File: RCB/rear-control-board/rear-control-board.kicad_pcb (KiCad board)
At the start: 2 copper layers, 53 parts, among them J1 Conn_01x23, J2 Conn_01x14, J3 Conn_01x08, J4 Conn_01x02, J5 Conn_01x02, J6 Conn_01x05, K1 T9VV1K15-12S, K2 G5V-2, K3 G5V-2, Q1 BSS84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

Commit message: working on layout
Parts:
- moved J3 161.0 mm to (97.5, 49.5), turned to 180 degrees
- moved F1 119.5 mm to (127.8, 72.1)
- moved F8 119.0 mm to (137.7, 97.6), turned to 180 degrees
- moved J2 111.4 mm to (145.0, 49.8), turned to 180 degrees
- moved C1 109.3 mm to (243.8, 101.6)
- moved C10 109.3 mm to (234.4, 103.4)
- moved C11 109.3 mm to (243.8, 94.1)
- moved C12 109.3 mm to (230.1, 103.4)
- moved C2 109.3 mm to (252.8, 93.9)
- moved C3 109.3 mm to (248.2, 96.4)
- moved C4 109.3 mm to (243.8, 99.1)
- moved C5 109.3 mm to (252.8, 91.4)
- moved C6 109.3 mm to (243.8, 96.6)
- moved C7 109.3 mm to (238.8, 103.4)
- moved C8 109.3 mm to (248.4, 93.9)
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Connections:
- F8 pad 1: +12V -> /SSOK
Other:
- board outline added: 99.1 x 99.1 mm

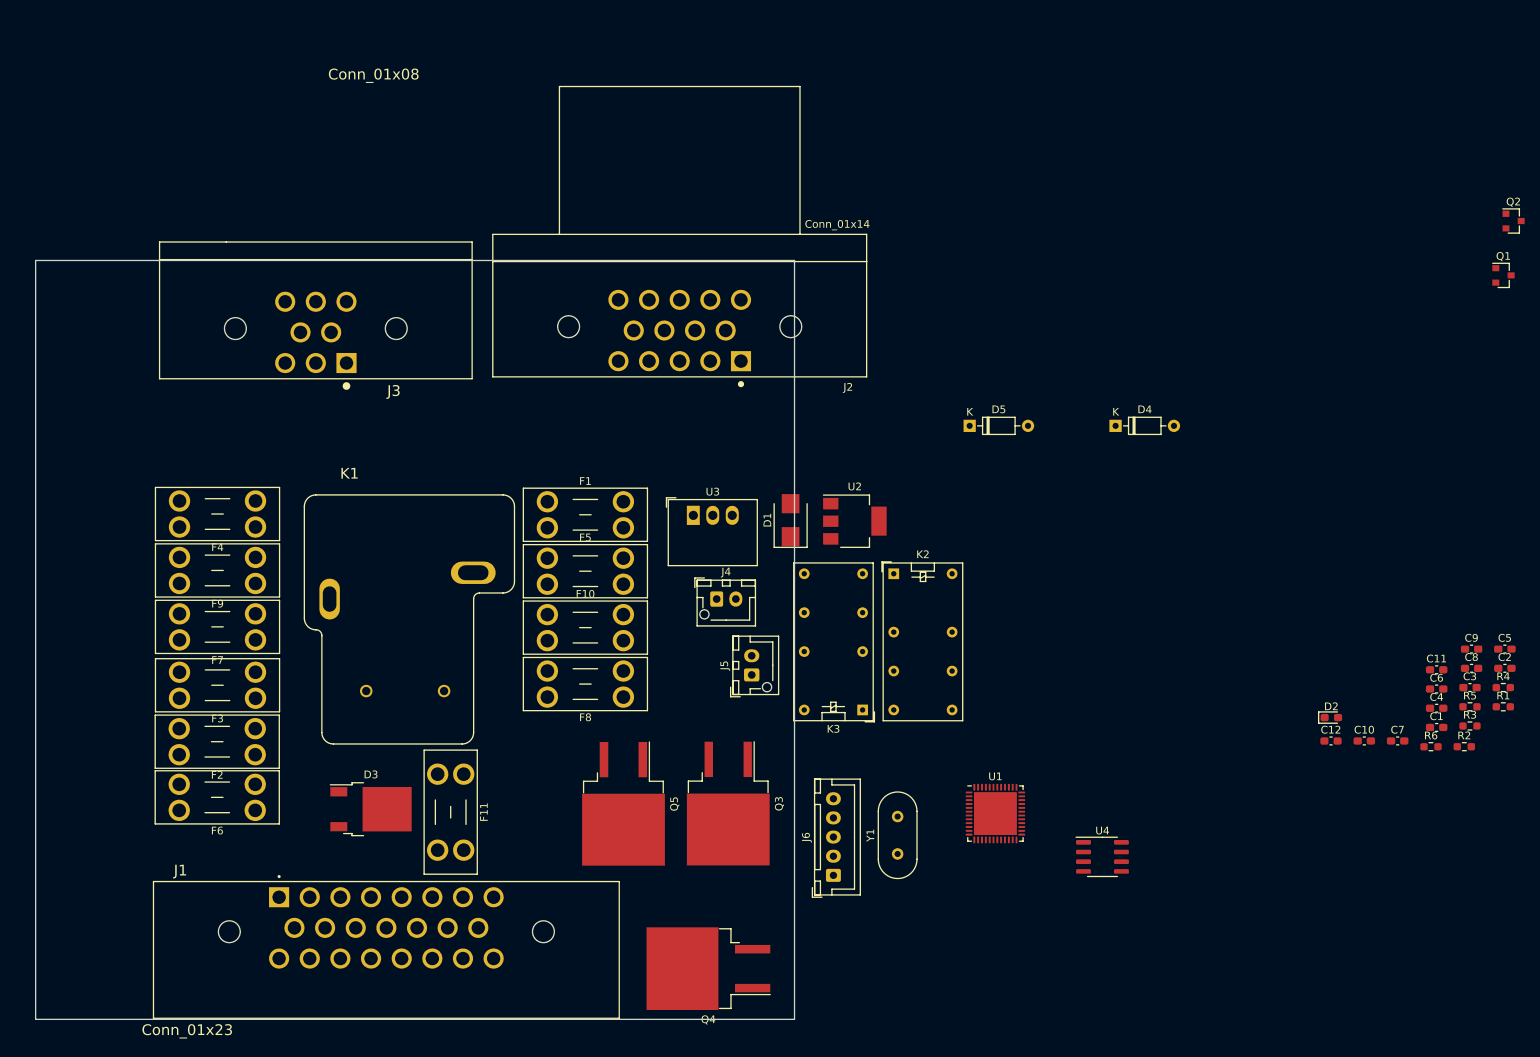
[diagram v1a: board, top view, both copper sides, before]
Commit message: layout and connector pins
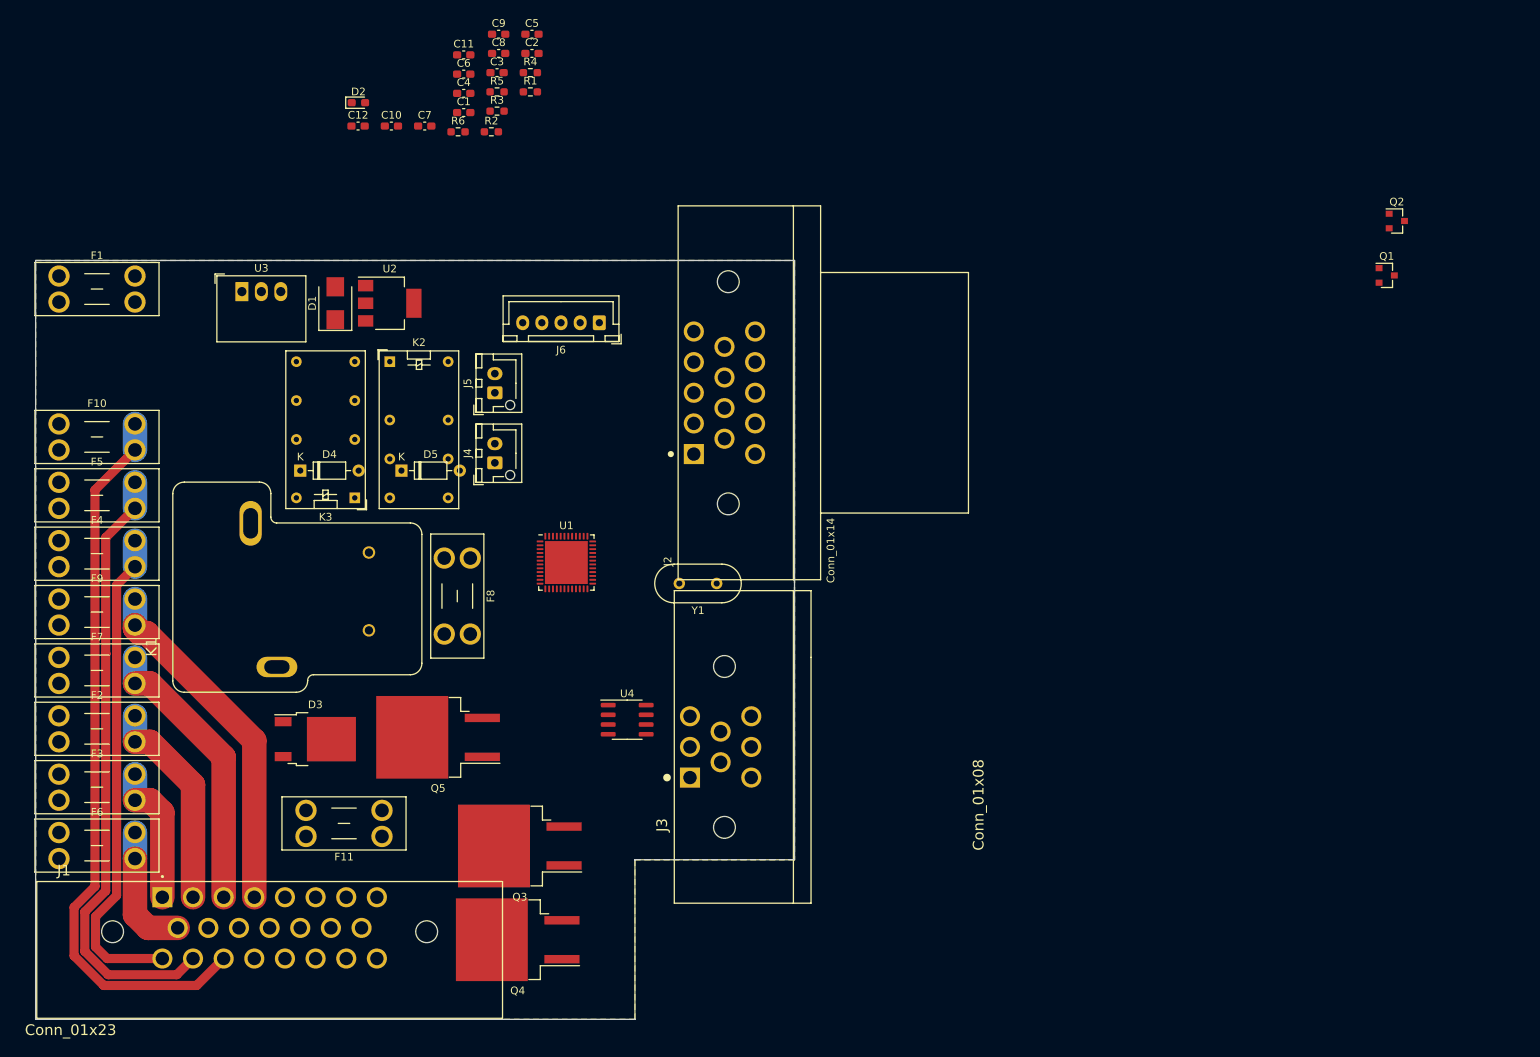
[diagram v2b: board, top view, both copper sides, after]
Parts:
- moved C12 150.2 mm to (103.0, 23.1)
- moved C1 150.2 mm to (116.8, 21.3)
- moved C10 150.2 mm to (107.4, 23.1)
- moved C11 150.2 mm to (116.8, 13.8)
- moved C2 150.2 mm to (125.8, 13.6)
- moved C3 150.2 mm to (121.2, 16.1)
- moved C4 150.2 mm to (116.8, 18.8)
- moved C5 150.2 mm to (125.8, 11.1)
- moved C6 150.2 mm to (116.8, 16.3)
- moved C7 150.2 mm to (111.8, 23.1)
- moved C8 150.2 mm to (121.4, 13.6)
- moved C9 150.2 mm to (121.4, 11.1)
- moved D2 150.2 mm to (103.1, 20.0)
- moved R1 150.2 mm to (125.5, 18.6)
- moved R2 150.2 mm to (120.5, 23.8)
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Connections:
- J1 pad 1: +12VA -> /RINEHART
- J1 pad 10: /PUMP_12V -> /FAULT_IMD
- J1 pad 11: /PUMP_SIG -> +12VA
- J1 pad 12: /RINEHART -> +12VA
- J1 pad 13: /DASH -> /DCDC_IN
- J1 pad 14: /HVB_12V -> /DCDC_IN
- J1 pad 15: /SPARE -> /PUMP_SIG
- J1 pad 16: /TSV -> /DASH
- J1 pad 17: /BRB -> /HVB_12V
- J1 pad 18: /BRB_RTN -> /BRB
- J1 pad 19: /FAULT_IMD -> /BRB_RTN
- J1 pad 2: +12VA -> /FAN_12V
- J1 pad 20: /FAULT_BMS -> GND
- J1 pad 21: Net-(J1-Pad21) -> GND
- J1 pad 22: GND -> /FAULT_BMS
- J1 pad 23: GND -> /TSV
- J1 pad 3: /DCDC_IN -> /SPARE
- J1 pad 4: /DCDC_IN -> /BRAKE_12V
- J1 pad 5: /DCDC_IN -> +12VA
- J1 pad 6: /FAN_12V -> /DCDC_IN
- J1 pad 7: /FAN_SIG -> /BRAKE_SIG
- J1 pad 8: /BRAKE_12V -> /FAN_SIG
- J1 pad 9: /BRAKE_SIG -> /PUMP_12V
- J3 pad 1: /CAN_P -> Net-(J3-Pad1)
- J3 pad 2: /CAN_P -> /CAN_N
- J3 pad 3: /CAN_N -> /CAN_P
- J3 pad 5: Net-(J3-Pad5) -> /CAN_P
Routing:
- net /BRB: track 0.00 -> 95.3 mm
- net /HVB_12V: track 0.00 -> 80.2 mm
- net /DASH: track 0.00 -> 64.5 mm
- net /BRAKE_12V: track 0.00 -> 45.9 mm
- net /SPARE: track 0.00 -> 37.3 mm
- net /FAN_12V: track 0.00 -> 28.0 mm
- net /RINEHART: track 0.00 -> 18.7 mm
- net /PUMP_12V: track 0.00 -> 17.0 mm
- added copper zone on B.Cu, net GND
- added copper zone on F.Cu, net GND
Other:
- outline, holes or cut-outs redrawn

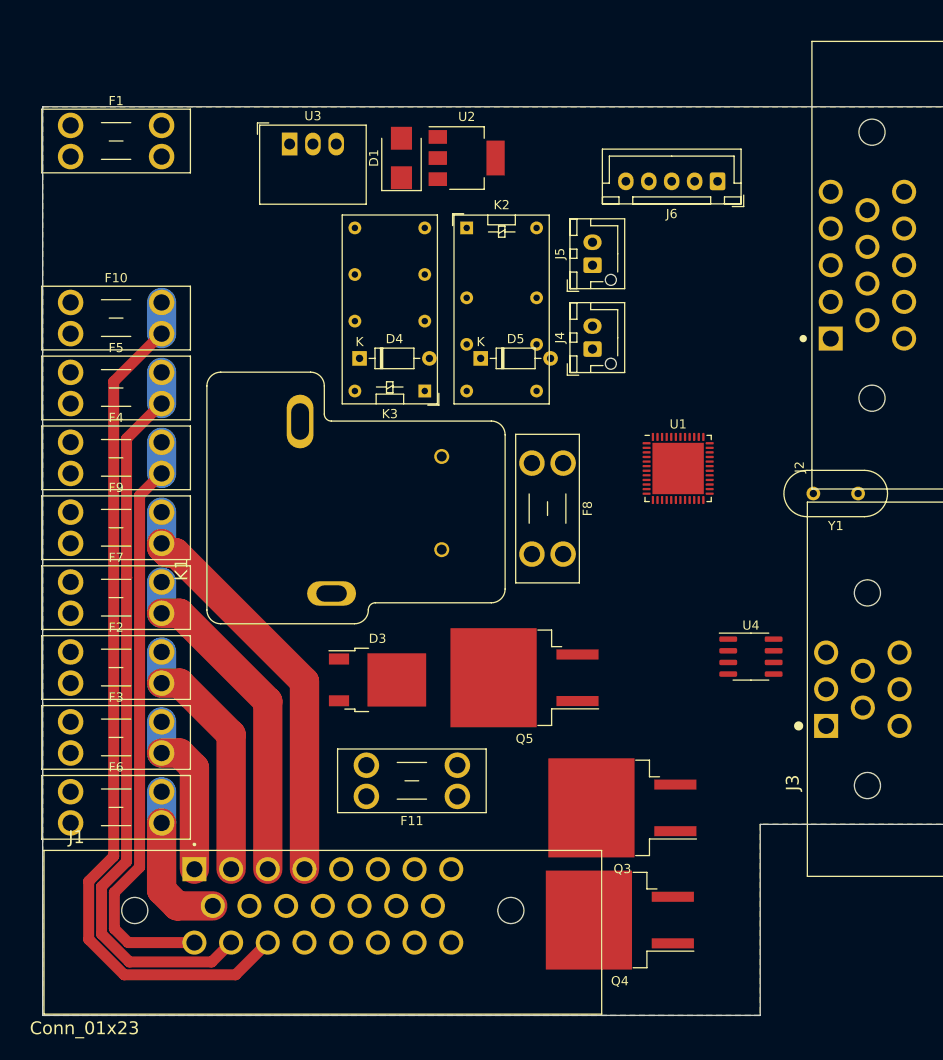
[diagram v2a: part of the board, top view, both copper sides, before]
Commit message: working on layout
Updating traces for RCB and organizing HVB
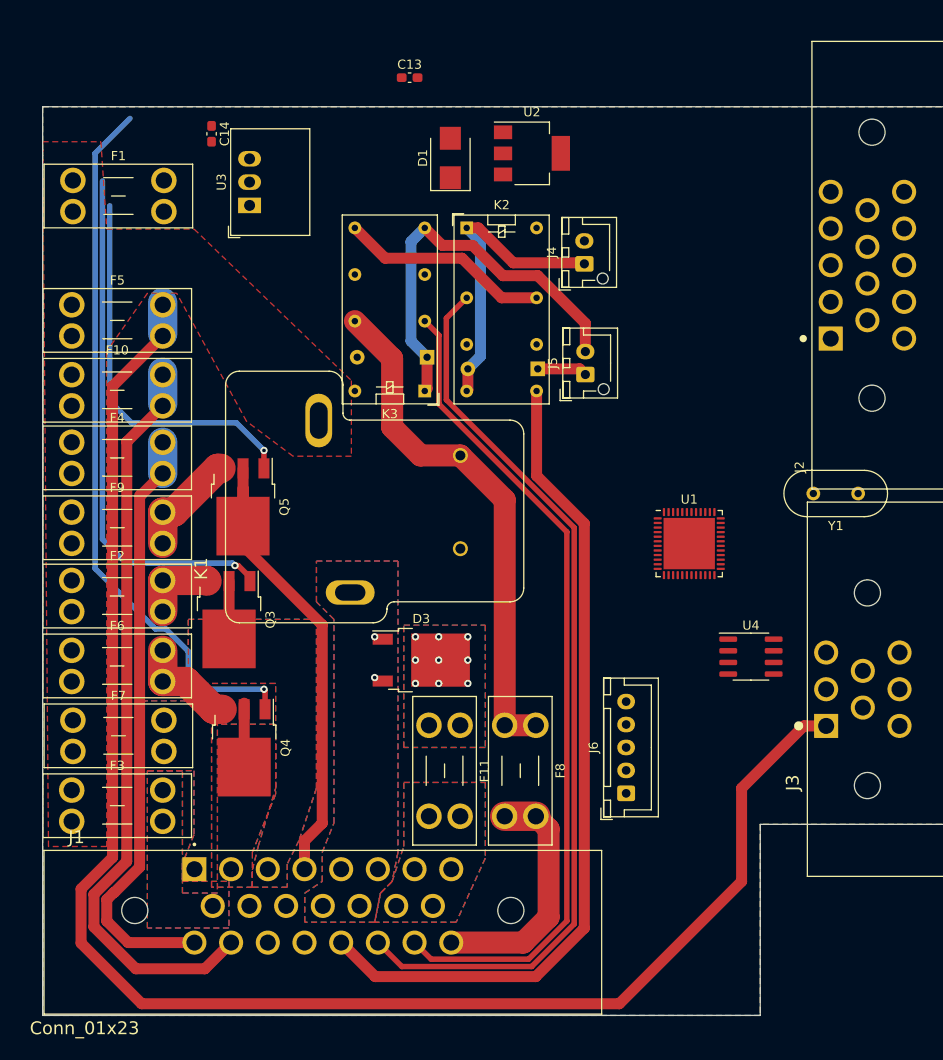
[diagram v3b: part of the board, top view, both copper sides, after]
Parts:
- added C13: C, Capacitor_SMD:C_0603_1608Metric_Pad1.08x0.95mm_HandSolder, F.Cu at (101.0, 37.5)
- added C14: C, Capacitor_SMD:C_0603_1608Metric_Pad1.08x0.95mm_HandSolder, F.Cu at (79.4, 43.6)
- D4, D5: moved to B.Cu
- Q3, Q4, Q5: value STB15N80K5 -> Q_PMOS_GDSD; footprint Package_TO_SOT_SMD:TO-263-2 -> Package_TO_SOT_SMD:TO-252-3_TabPin4
- moved J6 67.5 mm to (124.6, 115.5), turned to 90 degrees
- moved Q3 47.5 mm to (81.3, 96.6), turned to -90 degrees
- moved Q4 45.1 mm to (82.9, 110.5), turned to -90 degrees
- moved Q5 35.9 mm to (82.8, 84.3), turned to -90 degrees
- moved F8 28.7 mm to (114.7, 108.1)
- moved D4 19.5 mm to (114.9, 69.2), turned to 180 degrees
- moved F6 15.4 mm to (64.1, 99.9)
- moved F7 15.1 mm to (64.3, 107.5)
- moved J5 11.9 mm to (120.1, 69.8)
- moved J4 9.33 mm to (120.0, 57.8)
- moved U1 8.28 mm to (131.4, 88.3)
- moved U3 7.99 mm to (83.5, 51.4), turned to 90 degrees
- moved F10 7.87 mm to (64.1, 69.8)
- moved F2 7.80 mm to (64.1, 92.3)
- moved F11 7.76 mm to (106.5, 108.1), turned to -90 degrees
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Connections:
- net /FAULT_LATCHER/BMS_IND renamed /Controller/FAULT_BMS
- net Net-(D3-Pad2) renamed /charge-controller/dcdc_fuse
- net Net-(D4-Pad2) renamed /FAULT_LATCHER/bms_switch
- net Net-(D5-Pad1) renamed /FAULT_LATCHER/imd_switch
- net Net-(J3-Pad6) renamed /NC
- net Net-(K2-Pad13) renamed /FAULT_LATCHER/connector
- J1 pad 1: /RINEHART -> /SPARE
- J1 pad 10: /FAULT_IMD -> GND
- J1 pad 11: +12VA -> GND
- J1 pad 13: /DCDC_IN -> +12VA
- J1 pad 15: /PUMP_SIG -> /DCDC_IN
- J1 pad 17: /HVB_12V -> /BRB
- J1 pad 18: /BRB -> GND
- J1 pad 19: /BRB_RTN -> GND
- J1 pad 2: /FAN_12V -> /PUMP_CTRL_12V
- J1 pad 20: GND -> /BRB_RTN
- J1 pad 21: GND -> /FAULT_IMD
- J1 pad 3: /SPARE -> /FAN_CTRL_12V
- J1 pad 4: /BRAKE_12V -> /BRAKE_CTRL_12V
- J1 pad 6: /DCDC_IN -> +12VA
- J1 pad 7: /BRAKE_SIG -> /DCDC_IN
- J1 pad 8: /FAN_SIG -> /DCDC_IN
- J1 pad 9: /PUMP_12V -> /RINEHART
- J2 pad 13: +5V -> VDD
- J2 pad 14: +5V -> VDD
- J2 pad 5: GND -> unconnected-(J2-Pad5)
- J2 pad 6: +3V3 -> /TEMP_WATER
- J3 pad 1: Net-(J3-Pad1) -> /HVB_12V
- J3 pad 7: Net-(J3-Pad7) -> GND
- J3 pad 8: Net-(J3-Pad8) -> GND
- K2 pad 11: Net-(K2-Pad11) -> unconnected-(K2-Pad11)
- K2 pad 6: Net-(K2-Pad6) -> unconnected-(K2-Pad6)
- K3 pad 11: Net-(K3-Pad11) -> unconnected-(K3-Pad11)
- K3 pad 6: Net-(K3-Pad6) -> unconnected-(K3-Pad6)
- Q3 pad 2: /FAN_SIG -> /FAN_CTRL_12V
- Q3 pad 3: GND -> /FAN_12V
- Q4 pad 2: /PUMP_SIG -> /PUMP_CTRL_12V
- Q4 pad 3: GND -> /PUMP_12V
- Q5 pad 2: /BRAKE_SIG -> /BRAKE_CTRL_12V
- Q5 pad 3: GND -> /BRAKE_12V
- U1 pad 1: Net-(U1-Pad1) -> unconnected-(U1-Pad1)
- U1 pad 17: +3V3 -> /Controller/NTC1
- U1 pad 18: Net-(U1-Pad18) -> unconnected-(U1-Pad18)
- U1 pad 19: Net-(U1-Pad19) -> unconnected-(U1-Pad19)
- U1 pad 2: Net-(U1-Pad2) -> unconnected-(U1-Pad2)
- U1 pad 20: Net-(U1-Pad20) -> unconnected-(U1-Pad20)
- U1 pad 21: Net-(U1-Pad21) -> unconnected-(U1-Pad21)
- U1 pad 22: Net-(U1-Pad22) -> unconnected-(U1-Pad22)
- U1 pad 25: Net-(U1-Pad25) -> unconnected-(U1-Pad25)
- U1 pad 26: Net-(U1-Pad26) -> unconnected-(U1-Pad26)
- U1 pad 27: Net-(U1-Pad27) -> unconnected-(U1-Pad27)
- U1 pad 28: Net-(U1-Pad28) -> unconnected-(U1-Pad28)
- U1 pad 29: Net-(U1-Pad29) -> unconnected-(U1-Pad29)
- U1 pad 3: Net-(U1-Pad3) -> unconnected-(U1-Pad3)
- U1 pad 30: Net-(U1-Pad30) -> unconnected-(U1-Pad30)
- U1 pad 31: Net-(U1-Pad31) -> unconnected-(U1-Pad31)
- U1 pad 32: Net-(U1-Pad32) -> unconnected-(U1-Pad32)
- U1 pad 33: Net-(U1-Pad33) -> unconnected-(U1-Pad33)
- U1 pad 4: Net-(U1-Pad4) -> unconnected-(U1-Pad4)
- U1 pad 40: Net-(U1-Pad40) -> unconnected-(U1-Pad40)
- U1 pad 41: Net-(U1-Pad41) -> unconnected-(U1-Pad41)
- U1 pad 42: Net-(U1-Pad42) -> unconnected-(U1-Pad42)
- U1 pad 46: Net-(U1-Pad46) -> unconnected-(U1-Pad46)
- U1 pad 8: Net-(U1-Pad8) -> unconnected-(U1-Pad8)
- U4 pad 5: Net-(U4-Pad5) -> unconnected-(U4-Pad5)
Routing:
- net /FAULT_IMD: track 0.00 -> 99.4 mm
- net /HVB_12V: track 80.2 -> 175.7 mm
- net /BRB_RTN: track 0.00 -> 90.9 mm
- net /FAULT_BMS: track 0.00 -> 90.9 mm
- net /Controller/PUMP_CTRL: track 0.00 -> 78.0 mm, vias 0 -> 1
- net /Controller/FAN_CTRL: track 0.00 -> 57.3 mm, vias 0 -> 1
- net /SSOK: track 0.00 -> 56.8 mm
- net /BRAKE_CTRL_12V: track 0.00 -> 52.2 mm
- net /FAULT_LATCHER/imd_switch: track 0.00 -> 44.1 mm
- net /Controller/BRAKE_CTRL: track 0.00 -> 42.3 mm, vias 0 -> 1
- net /SPARE: track 37.3 -> 0.00 mm
- net /BRAKE_12V: track 45.9 -> 11.7 mm
- net /FAULT_LATCHER/bms_switch: track 0.00 -> 33.5 mm
- net /TSV: track 0.00 -> 26.7 mm
- net /FAULT_LATCHER/connector: track 0.00 -> 23.0 mm
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- added copper zone on F.Cu, net +12V
- added copper zone on B.Cu, net +12VA
- added copper zone on F.Cu, net +12VA
- added copper zone on B.Cu, net /DCDC_IN
- added copper zone on F.Cu, net /DCDC_IN
- added copper zone on B.Cu, net /FAN_CTRL_12V
- added copper zone on F.Cu, net /FAN_CTRL_12V
- added copper zone on B.Cu, net /PUMP_CTRL_12V
- added copper zone on F.Cu, net /PUMP_CTRL_12V
- added copper zone on B.Cu, net /RINEHART
- added copper zone on F.Cu, net /RINEHART
- added copper zone on B.Cu, net /SPARE
- added copper zone on F.Cu, net /SPARE
- added copper zone on B.Cu, net /charge-controller/dcdc_fuse
- added copper zone on F.Cu, net /charge-controller/dcdc_fuse
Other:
- net class Default removed
